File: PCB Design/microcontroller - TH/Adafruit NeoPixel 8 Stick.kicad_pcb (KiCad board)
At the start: 2 copper layers, 34.5 x 47.5 mm, 6 parts, among them CN2 1X4SMT, U1 ATmega328P-P, Y1 Crystal_Small

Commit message: changed pcbs
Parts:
- added R1: R, Resistor_THT:R_Axial_DIN0207_L6.3mm_D2.5mm_P7.62mm_Horizontal, F.Cu at (131.1, 110.2)
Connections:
- U1 pad 1: GND -> Net-(U1-Pad1)
- U1 pad 20: +5V -> unconnected-(U1-Pad20)
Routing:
- net Net-(U1-Pad1): track 0.00 -> 14.4 mm, vias 0 -> 1
- net +5V: track 41.4 -> 34.9 mm
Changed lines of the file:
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@@
   (net 24 "unconnected-(U1-Pad25)")
   (net 25 "unconnected-(U1-Pad26)")
+  (net 26 "Net-(U1-Pad1)")
+  (net 27 "unconnected-(U1-Pad20)")
   (footprint "Crystal:Crystal_HC49-U_Vertical" (layer "F.Cu")
     (at 135.382 125.64 90)
@@
     (fp_line (start 6.985 -1.27) (end 6.985 34.29) (layer "F.Fab") (width 0.1))
     (pad "1" thru_hole rect (at 0 0) (size 1.6 1.6) (drill 0.8) (layers *.Cu *.Mask)
-      (net 2 "GND") (pinfunction "~{RESET}/PC6") (pintype "bidirectional"))
+      (net 26 "Net-(U1-Pad1)") (pinfunction "~{RESET}/PC6") (pintype "bidirectional"))
     (pad "2" thru_hole oval (at 0 2.54) (size 1.6 1.6) (drill 0.8) (layers *.Cu *.Mask)
       (net 6 "unconnected-(U1-Pad2)") (pinfunction "PD0") (pintype "bidirectional"))
@@
       (net 20 "unconnected-(U1-Pad19)") (pinfunction "PB5") (pintype "bidirectional"))
     (pad "20" thru_hole oval (at 7.62 20.32) (size 1.6 1.6) (drill 0.8) (layers *.Cu *.Mask)
-      (net 1 "+5V") (pinfunction "AVCC") (pintype "power_in"))
+      (net 27 "unconnected-(U1-Pad20)") (pinfunction "AVCC") (pintype "power_in"))
     (pad "21" thru_hole oval (at 7.62 17.78) (size 1.6 1.6) (drill 0.8) (layers *.Cu *.Mask)
       (net 21 "unconnected-(U1-Pad21)") (pinfunction "AREF") (pintype "passive"))
@@
     )
   )
+  (footprint "Resistor_THT:R_Axial_DIN0207_L6.3mm_D2.5mm_P7.62mm_Horizontal" (layer "F.Cu")
+    (at 131.064 110.236 90)
+    (descr "Resistor, Axial_DIN0207 series, Axial, Horizontal, pin pitch=7.62mm, 0.25W = 1/4W, length*diameter=6.3*2.5mm^2, http://cdn-reichelt.de/documents/datenblatt/B400/1_4W%23YAG.pdf")
+    (tags "Resistor Axial_DIN0207 series Axial Horizontal pin pitch 7.62mm 0.25W = 1/4W length 6.3mm diameter 2.5mm")
+    (property "Sheetfile" "Adafruit NeoPixel 8 Stick.kicad_sch")
+    (property "Sheetname" "")
+    (attr through_hole)
+    (fp_text reference "R1" (at 3.81 -2.37 90) (layer "F.SilkS")
+      (effects (font (size 1 1) (thickness 0.15)))
+    )
+    (fp_text value "R" (at -1.975656 -0.538815 90) (layer "F.Fab")
+      (effects (font (size 1 1) (thickness 0.15)))
+    )
+    (fp_text user "${REFERENCE}" (at 3.81 0 90) (layer "F.Fab")
+      (effects (font (size 1 1) (thickness 0.15)))
+    )
+    (fp_line (start 0.54 1.04) (end 0.54 1.37) (layer "F.SilkS") (width 0.12))
+    (fp_line (start 7.08 1.37) (end 7.08 1.04) (layer "F.SilkS") (width 0.12))
+    (fp_line (start 0.54 -1.37) (end 7.08 -1.37) (layer "F.SilkS") (width 0.12))
+    (fp_line (start 0.54 -1.04) (end 0.54 -1.37) (layer "F.SilkS") (width 0.12))
+    (fp_line (start 0.54 1.37) (end 7.08 1.37) (layer "F.SilkS") (width 0.12))
+    (fp_line (start 7.08 -1.37) (end 7.08 -1.04) (layer "F.SilkS") (width 0.12))
+    (fp_line (start 8.67 -1.5) (end -1.05 -1.5) (layer "F.CrtYd") (width 0.05))
+    (fp_line (start 8.67 1.5) (end 8.67 -1.5) (layer "F.CrtYd") (width 0.05))
+    (fp_line (start -1.05 1.5) (end 8.67 1.5) (layer "F.CrtYd") (width 0.05))
+    (fp_line (start -1.05 -1.5) (end -1.05 1.5) (layer "F.CrtYd") (width 0.05))
+    (fp_line (start 0.66 -1.25) (end 0.66 1.25) (layer "F.Fab") (width 0.1))
+    (fp_line (start 6.96 1.25) (end 6.96 -1.25) (layer "F.Fab") (width 0.1))
+    (fp_line (start 0 0) (end 0.66 0) (layer "F.Fab") (width 0.1))
+    (fp_line (start 7.62 0) (end 6.96 0) (layer "F.Fab") (width 0.1))
+    (fp_line (start 0.66 1.25) (end 6.96 1.25) (layer "F.Fab") (width 0.1))
+    (fp_line (start 6.96 -1.25) (end 0.66 -1.25) (layer "F.Fab") (width 0.1))
+    (pad "1" thru_hole circle (at 0 0 90) (size 1.6 1.6) (drill 0.8) (layers *.Cu *.Mask)
+      (net 1 "+5V") (pintype "passive"))
+    (pad "2" thru_hole oval (at 7.62 0 90) (size 1.6 1.6) (drill 0.8) (layers *.Cu *.Mask)
+      (net 26 "Net-(U1-Pad1)") (pintype "passive"))
+    (model "${KICAD6_3DMODEL_DIR}/Resistor_THT.3dshapes/R_Axial_DIN0207_L6.3mm_D2.5mm_P7.62mm_Horizontal.wrl"
+      (offset (xyz 0 0 0))
+      (scale (xyz 1 1 1))
+      (rotate (xyz 0 0 0))
+    )
+  )
   (footprint "Adafruit NeoPixel 8 Stick:1X4-SMT" (layer "B.Cu")
     (at 139.954 93.726 180)
@@
   (gr_line (start 156.972 97.45) (end 156.972 137.414) (layer "Edge.Cuts") (width 0.05))
   (gr_line (start 122.428 97.536) (end 129.2 89.916) (layer "Edge.Cuts") (width 0.05))
-  (segment (start 144.79 116.342) (end 147.33 116.342) (width 0.25) (layer "F.Cu") (net 1))
   (segment (start 138.644 110.196) (end 144.79 116.342) (width 0.25) (layer "F.Cu") (net 1))
   (segment (start 138.644 99.1) (end 144.018 93.726) (width 0.25) (layer "F.Cu") (net 1))
   (segment (start 134.366 110.196) (end 138.644 110.196) (width 0.25) (layer "F.Cu") (net 1))
+  (segment (start 131.064 110.236) (end 134.326 110.236) (width 0.25) (layer "F.Cu") (net 1))
   (segment (start 138.644 110.196) (end 138.644 99.1) (width 0.25) (layer "F.Cu") (net 1))
-  (segment (start 147.33 116.342) (end 152.41 121.422) (width 0.25) (layer "F.Cu") (net 1))
   (via (at 144.018 93.726) (size 0.8) (drill 0.4) (layers "F.Cu" "B.Cu") (net 1))
   (segment (start 140.874 104.806) (end 140.874 93.726) (width 0.25) (layer "B.Cu") (net 3))
@@
   (segment (start 129.754 125.984) (end 135.038 125.984) (width 0.25) (layer "F.Cu") (net 11))
   (segment (start 135.382 125.64) (end 143.112 125.64) (width 0.25) (layer "F.Cu") (net 11))
+  (segment (start 144.79 101.102) (end 140.6112 101.102) (width 0.25) (layer "F.Cu") (net 26))
+  (segment (start 140.6112 101.102) (end 139.3986 102.3146) (width 0.25) (layer "F.Cu") (net 26))
+  (via (at 139.3986 102.3146) (size 0.8) (drill 0.4) (layers "F.Cu" "B.Cu") (net 26))
+  (segment (start 139.0972 102.616) (end 131.064 102.616) (width 0.25) (layer "B.Cu") (net 26))
+  (segment (start 139.3986 102.3146) (end 139.0972 102.616) (width 0.25) (layer "B.Cu") (net 26))
   (zone (net 2) (net_name "GND") (layers F&B.Cu) (hatch edge 0.508)
     (connect_pads (clearance 0.000001))

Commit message: updated some pcbs
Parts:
- added D1: LED_Small_Filled, LED_THT:LED_D3.0mm, F.Cu at (125.7, 129.0)
- added R2: R, Resistor_THT:R_Axial_DIN0207_L6.3mm_D2.5mm_P7.62mm_Horizontal, F.Cu at (131.8, 129.8)
- moved C3 3.81 mm to (124.8, 116.8)
- moved Y1 3.81 mm to (135.4, 121.8)
- moved C2 3.81 mm to (124.8, 122.2)
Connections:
- U1 pad 19: unconnected-(U1-Pad19) -> Net-(U1-Pad19)
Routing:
- net Net-(U1-Pad19): track 0.00 -> 24.9 mm
- net Net-(D1-Pad2): track 0.00 -> 3.81 mm
- net Net-(C3-Pad2): track 15.2 -> 16.8 mm

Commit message: clean up boards + generate some gerber files
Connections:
- net Net-(CN2-Pad3) renamed /LED DATA
- net Net-(CN2-Pad5) renamed /SDA
- net Net-(CN2-Pad6) renamed /SCL

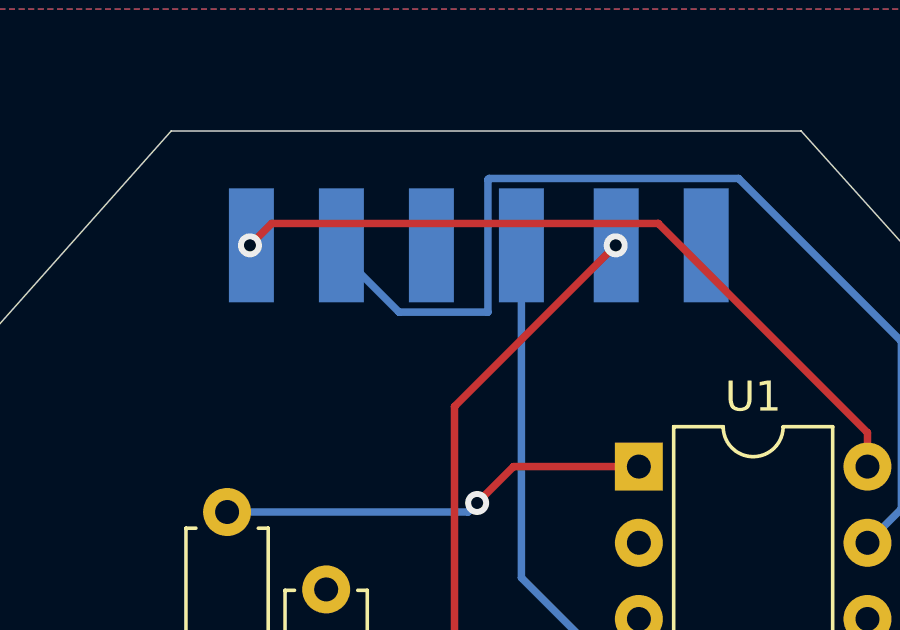
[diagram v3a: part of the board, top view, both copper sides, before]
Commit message: rm vias over pads
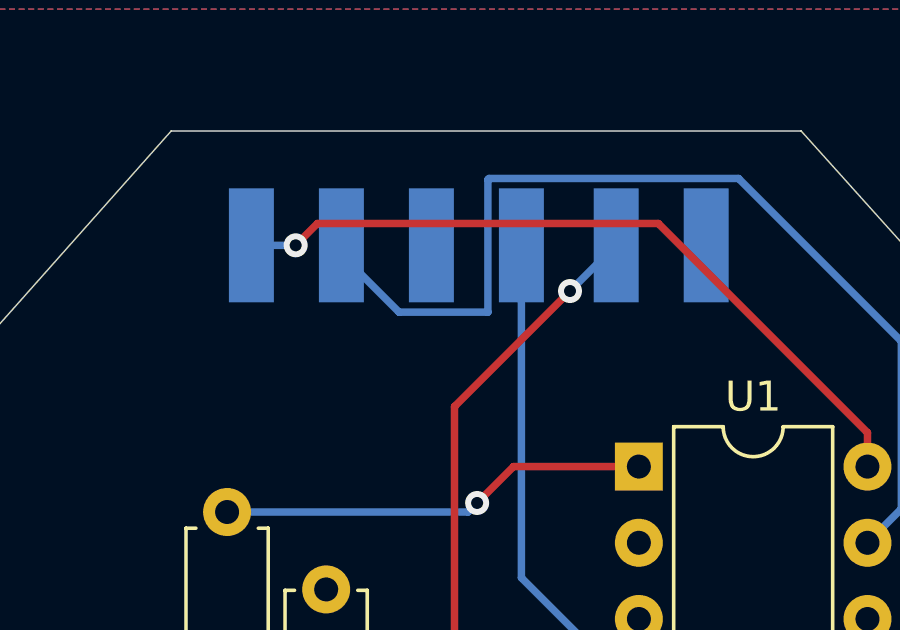
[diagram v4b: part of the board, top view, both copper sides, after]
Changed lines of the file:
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@@
   (gr_line (start 122.428 97.536) (end 129.2 89.916) (layer "Edge.Cuts") (width 0.05))
   (segment (start 138.644 110.196) (end 144.79 116.342) (width 0.25) (layer "F.Cu") (net 1))
-  (segment (start 138.644 99.1) (end 144.018 93.726) (width 0.25) (layer "F.Cu") (net 1))
   (segment (start 134.366 110.196) (end 138.644 110.196) (width 0.25) (layer "F.Cu") (net 1))
   (segment (start 131.064 110.236) (end 134.326 110.236) (width 0.25) (layer "F.Cu") (net 1))
   (segment (start 138.644 110.196) (end 138.644 99.1) (width 0.25) (layer "F.Cu") (net 1))
-  (via (at 144.018 93.726) (size 0.8) (drill 0.4) (layers "F.Cu" "B.Cu") (net 1))
+  (segment (start 138.644 99.1) (end 142.494 95.25) (width 0.25) (layer "F.Cu") (net 1))
+  (via (at 142.494 95.25) (size 0.8) (drill 0.4) (layers "F.Cu" "B.Cu") (net 1))
+  (segment (start 144.018 93.726) (end 142.494 95.25) (width 0.25) (layer "B.Cu") (net 1))
   (segment (start 140.874 104.806) (end 140.874 93.726) (width 0.25) (layer "B.Cu") (net 3))
   (segment (start 144.79 108.722) (end 140.874 104.806) (width 0.25) (layer "B.Cu") (net 3))
@@
   (segment (start 136.7958 95.9542) (end 139.7578 95.9542) (width 0.25) (layer "B.Cu") (net 4))
   (segment (start 134.874 94.0324) (end 136.7958 95.9542) (width 0.25) (layer "B.Cu") (net 4))
+  (segment (start 134.0782 92.9978) (end 133.35 93.726) (width 0.25) (layer "F.Cu") (net 5))
   (segment (start 152.41 99.97063) (end 145.43717 92.9978) (width 0.25) (layer "F.Cu") (net 5))
-  (segment (start 145.43717 92.9978) (end 132.5542 92.9978) (width 0.25) (layer "F.Cu") (net 5))
-  (segment (start 132.5542 92.9978) (end 131.826 93.726) (width 0.25) (layer "F.Cu") (net 5))
+  (segment (start 145.43717 92.9978) (end 134.0782 92.9978) (width 0.25) (layer "F.Cu") (net 5))
   (segment (start 152.41 101.102) (end 152.41 99.97063) (width 0.25) (layer "F.Cu") (net 5))
-  (via (at 131.826 93.726) (size 0.8) (drill 0.4) (layers "F.Cu" "B.Cu") (net 5))
+  (via (at 133.35 93.726) (size 0.8) (drill 0.4) (layers "F.Cu" "B.Cu") (net 5))
+  (segment (start 133.35 93.726) (end 131.874 93.726) (width 0.25) (layer "B.Cu") (net 5))
   (segment (start 129.754 116.84) (end 135.272 116.84) (width 0.25) (layer "F.Cu") (net 10))
   (segment (start 138.286 116.95) (end 142.758 121.422) (width 0.25) (layer "F.Cu") (net 10))
